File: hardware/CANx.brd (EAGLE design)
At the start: 34.6 x 29.1 mm, 13 parts, among them Q1 16MHz, U2 MCP2551SO8, X1 RJ45_RIGHT_ANGLEMOLEX_95001-2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, X2 RJ45_RIGHT_ANGLEMOLEX_95001-2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

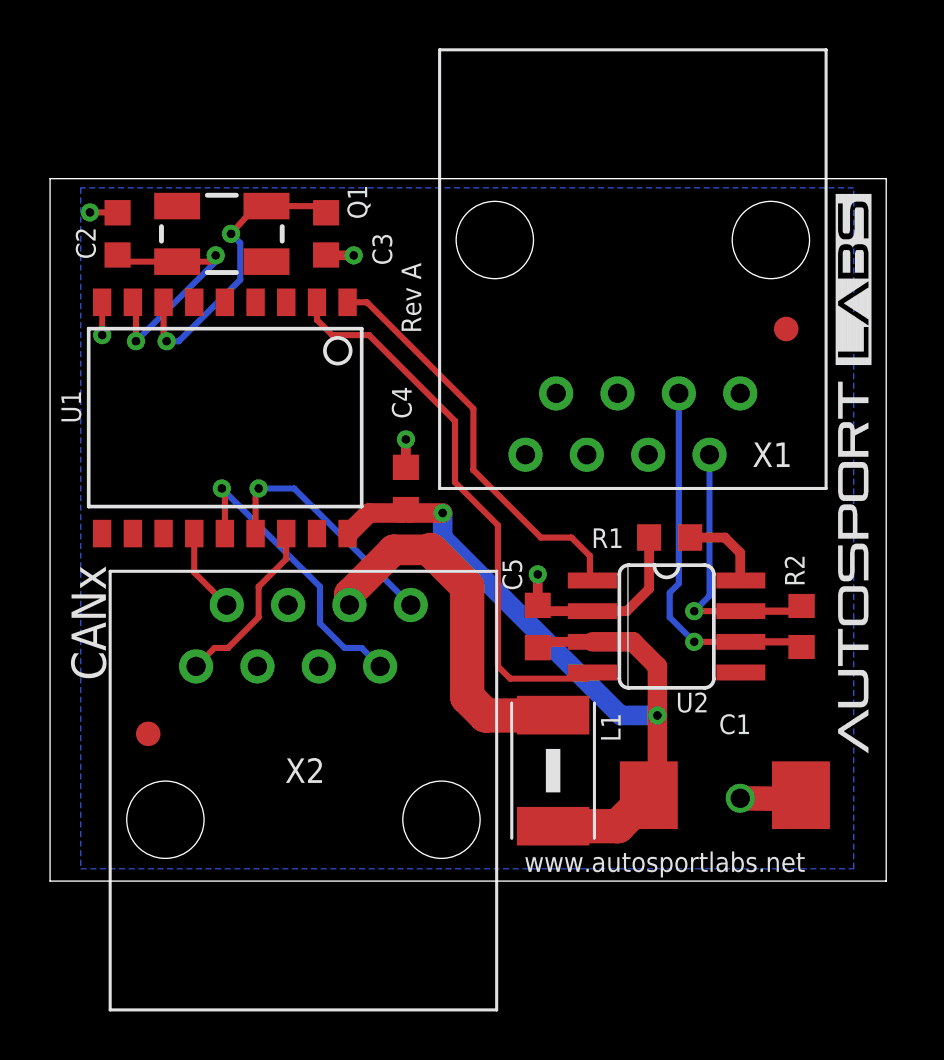
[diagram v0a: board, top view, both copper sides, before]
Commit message: updated CANx to use TSSOP-20 and center CAN connection plug to make it easier to identify orientation
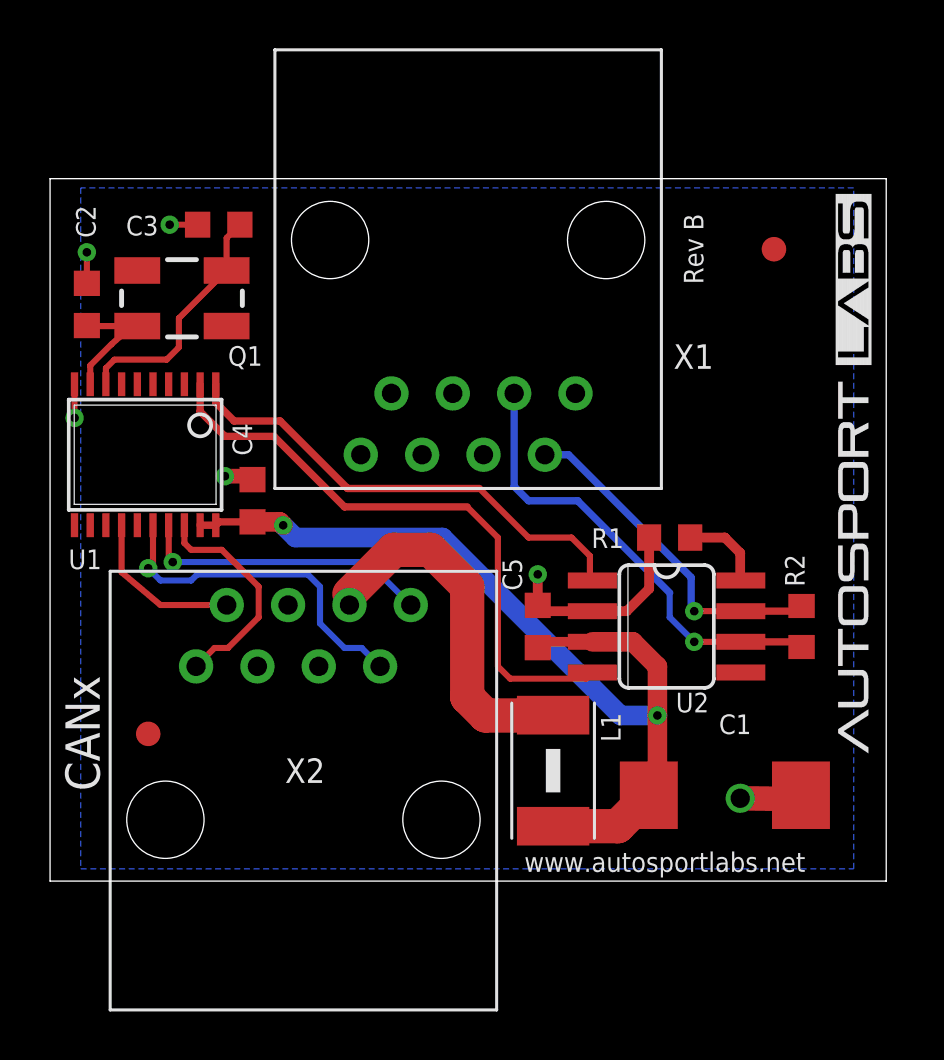
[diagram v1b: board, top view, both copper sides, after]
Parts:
- U1: device can:SO-18W -> can:TSSOP20
- moved X1 6.82 mm to (17.3, 26.5)
- moved C4 6.37 mm to (8.38, 15.7)
- moved C3 4.46 mm to (6.99, 27.2), turned to 180 degrees
- moved U1 3.64 mm to (3.94, 17.7)
- moved C2 3.19 mm to (1.52, 23.9)
- moved Q1 3.14 mm to (5.46, 24.1)
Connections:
- net +5V: now also U1.19, U1.20; no longer U1.18
- net GND: now also U1.10; no longer U1.9
- net MISO: now also U1.17; no longer U1.15
- net MOSI: now also U1.16; no longer U1.14
- net N$1: now also U1.9; no longer U1.8
- net N$2: now also U1.8; no longer U1.7
- net NPCS1: now also U1.18; no longer U1.16
- net SPCK: now also U1.14; no longer U1.13
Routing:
- net N$1: track 10.9 -> 5.44 mm, vias 2 -> 0
- net +5V: track 33.0 -> 38.0 mm
- net CANL: track 16.8 -> 20.5 mm
- net SPCK: track 3.52 -> 6.80 mm
- net CAN1_TX: track 16.9 -> 19.9 mm
- net CANH: track 12.0 -> 14.8 mm
- net N$2: track 12.4 -> 10.2 mm, vias 2 -> 0
- net MISO: track 10.2 -> 12.2 mm
- net NPCS1: track 7.37 -> 9.26 mm
- net CAN1_RX: track 23.3 -> 25.2 mm
- net MOSI: track 12.4 -> 14.3 mm
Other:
- board text added: "Rev B"
- board text removed: "Rev A"
